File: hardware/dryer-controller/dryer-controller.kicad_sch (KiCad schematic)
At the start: 69 parts, among them K1 SRD-05VDC-SL-C, K2 SRD-05VDC-SL-C, Q1 MMBT2222A, Q2 MMBT2222A, Q3 SI2308, Q4 SI2308, Q5 SI2308, SW1 SW-USB, U1 K7805-1000R3

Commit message: Export fab files, JLCPCB BOM and CPL, and review renders
Add an export command that writes the gerber zip with drill files, a JLCPCB
BOM and CPL, the schematic PDF, a top SVG and two 3D renders from the
committed project, and copies the four review files to docs/hardware.
Mounting holes are now excluded from the BOM so the fab BOM lists only parts.
README gains an Ordering section.

Co-Authored-By: Claude Sonnet 5.5 <noreply@anthropic.com>
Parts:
- H1, H2, H3, H4: now left out of the parts list
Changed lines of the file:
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@@
 (symbol (lib_id "Connector:TestPoint") (at 177.80 254.00 0) (unit 1) (exclude_from_sim no) (in_bom yes) (on_board yes) (dnp no) (property "Reference" "TP9" (at 177.80 251.46 0) (effects (font (size 1.27 1.27)))) (property "Value" "FAN" (at 177.80 256.54 0) (effects (font (size 1.27 1.27)))) (property "Footprint" "TestPoint:TestPoint_Pad_D1.5mm" (at 177.80 254.00 0) (effects (font (size 1.27 1.27)) (hide yes))) (property "Datasheet" "~" (at 177.80 254.00 0) (effects (font (size 1.27 1.27)) (hide yes))) (property "LCSC" "" (at 177.80 254.00 0) (effects (font (size 1.27 1.27)) (hide yes))) (property "Description" "" (at 177.80 254.00 0) (effects (font (size 1.27 1.27)) (hide yes))) (pin "1") (instances (project "dryer-controller" (path "/6edf3ea2-c7c9-5bc2-9303-ad80166c5e3e" (reference "TP9") (unit 1)))))
 (global_label "FAN" (shape input) (at 177.80 254.00 270) (effects (font (size 1.27 1.27)) (justify left)))
-(symbol (lib_id "Mechanical:MountingHole") (at 215.90 254.00 0) (unit 1) (exclude_from_sim no) (in_bom yes) (on_board yes) (dnp no) (property "Reference" "H1" (at 215.90 251.46 0) (effects (font (size 1.27 1.27)))) (property "Value" "M3" (at 215.90 256.54 0) (effects (font (size 1.27 1.27)))) (property "Footprint" "MountingHole:MountingHole_3.2mm_M3" (at 215.90 254.00 0) (effects (font (size 1.27 1.27)) (hide yes))) (property "Datasheet" "~" (at 215.90 254.00 0) (effects (font (size 1.27 1.27)) (hide yes))) (property "LCSC" "" (at 215.90 254.00 0) (effects (font (size 1.27 1.27)) (hide yes))) (property "Description" "" (at 215.90 254.00 0) (effects (font (size 1.27 1.27)) (hide yes)))  (instances (project "dryer-controller" (path "/6edf3ea2-c7c9-5bc2-9303-ad80166c5e3e" (reference "H1") (unit 1)))))
-(symbol (lib_id "Mechanical:MountingHole") (at 254.00 254.00 0) (unit 1) (exclude_from_sim no) (in_bom yes) (on_board yes) (dnp no) (property "Reference" "H2" (at 254.00 251.46 0) (effects (font (size 1.27 1.27)))) (property "Value" "M3" (at 254.00 256.54 0) (effects (font (size 1.27 1.27)))) (property "Footprint" "MountingHole:MountingHole_3.2mm_M3" (at 254.00 254.00 0) (effects (font (size 1.27 1.27)) (hide yes))) (property "Datasheet" "~" (at 254.00 254.00 0) (effects (font (size 1.27 1.27)) (hide yes))) (property "LCSC" "" (at 254.00 254.00 0) (effects (font (size 1.27 1.27)) (hide yes))) (property "Description" "" (at 254.00 254.00 0) (effects (font (size 1.27 1.27)) (hide yes)))  (instances (project "dryer-controller" (path "/6edf3ea2-c7c9-5bc2-9303-ad80166c5e3e" (reference "H2") (unit 1)))))
-(symbol (lib_id "Mechanical:MountingHole") (at 292.10 254.00 0) (unit 1) (exclude_from_sim no) (in_bom yes) (on_board yes) (dnp no) (property "Reference" "H3" (at 292.10 251.46 0) (effects (font (size 1.27 1.27)))) (property "Value" "M3" (at 292.10 256.54 0) (effects (font (size 1.27 1.27)))) (property "Footprint" "MountingHole:MountingHole_3.2mm_M3" (at 292.10 254.00 0) (effects (font (size 1.27 1.27)) (hide yes))) (property "Datasheet" "~" (at 292.10 254.00 0) (effects (font (size 1.27 1.27)) (hide yes))) (property "LCSC" "" (at 292.10 254.00 0) (effects (font (size 1.27 1.27)) (hide yes))) (property "Description" "" (at 292.10 254.00 0) (effects (font (size 1.27 1.27)) (hide yes)))  (instances (project "dryer-controller" (path "/6edf3ea2-c7c9-5bc2-9303-ad80166c5e3e" (reference "H3") (unit 1)))))
-(symbol (lib_id "Mechanical:MountingHole") (at 330.20 254.00 0) (unit 1) (exclude_from_sim no) (in_bom yes) (on_board yes) (dnp no) (property "Reference" "H4" (at 330.20 251.46 0) (effects (font (size 1.27 1.27)))) (property "Value" "M3" (at 330.20 256.54 0) (effects (font (size 1.27 1.27)))) (property "Footprint" "MountingHole:MountingHole_3.2mm_M3" (at 330.20 254.00 0) (effects (font (size 1.27 1.27)) (hide yes))) (property "Datasheet" "~" (at 330.20 254.00 0) (effects (font (size 1.27 1.27)) (hide yes))) (property "LCSC" "" (at 330.20 254.00 0) (effects (font (size 1.27 1.27)) (hide yes))) (property "Description" "" (at 330.20 254.00 0) (effects (font (size 1.27 1.27)) (hide yes)))  (instances (project "dryer-controller" (path "/6edf3ea2-c7c9-5bc2-9303-ad80166c5e3e" (reference "H4") (unit 1)))))
+(symbol (lib_id "Mechanical:MountingHole") (at 215.90 254.00 0) (unit 1) (exclude_from_sim no) (in_bom no) (on_board yes) (dnp no) (property "Reference" "H1" (at 215.90 251.46 0) (effects (font (size 1.27 1.27)))) (property "Value" "M3" (at 215.90 256.54 0) (effects (font (size 1.27 1.27)))) (property "Footprint" "MountingHole:MountingHole_3.2mm_M3" (at 215.90 254.00 0) (effects (font (size 1.27 1.27)) (hide yes))) (property "Datasheet" "~" (at 215.90 254.00 0) (effects (font (size 1.27 1.27)) (hide yes))) (property "LCSC" "" (at 215.90 254.00 0) (effects (font (size 1.27 1.27)) (hide yes))) (property "Description" "" (at 215.90 254.00 0) (effects (font (size 1.27 1.27)) (hide yes)))  (instances (project "dryer-controller" (path "/6edf3ea2-c7c9-5bc2-9303-ad80166c5e3e" (reference "H1") (unit 1)))))
+(symbol (lib_id "Mechanical:MountingHole") (at 254.00 254.00 0) (unit 1) (exclude_from_sim no) (in_bom no) (on_board yes) (dnp no) (property "Reference" "H2" (at 254.00 251.46 0) (effects (font (size 1.27 1.27)))) (property "Value" "M3" (at 254.00 256.54 0) (effects (font (size 1.27 1.27)))) (property "Footprint" "MountingHole:MountingHole_3.2mm_M3" (at 254.00 254.00 0) (effects (font (size 1.27 1.27)) (hide yes))) (property "Datasheet" "~" (at 254.00 254.00 0) (effects (font (size 1.27 1.27)) (hide yes))) (property "LCSC" "" (at 254.00 254.00 0) (effects (font (size 1.27 1.27)) (hide yes))) (property "Description" "" (at 254.00 254.00 0) (effects (font (size 1.27 1.27)) (hide yes)))  (instances (project "dryer-controller" (path "/6edf3ea2-c7c9-5bc2-9303-ad80166c5e3e" (reference "H2") (unit 1)))))
+(symbol (lib_id "Mechanical:MountingHole") (at 292.10 254.00 0) (unit 1) (exclude_from_sim no) (in_bom no) (on_board yes) (dnp no) (property "Reference" "H3" (at 292.10 251.46 0) (effects (font (size 1.27 1.27)))) (property "Value" "M3" (at 292.10 256.54 0) (effects (font (size 1.27 1.27)))) (property "Footprint" "MountingHole:MountingHole_3.2mm_M3" (at 292.10 254.00 0) (effects (font (size 1.27 1.27)) (hide yes))) (property "Datasheet" "~" (at 292.10 254.00 0) (effects (font (size 1.27 1.27)) (hide yes))) (property "LCSC" "" (at 292.10 254.00 0) (effects (font (size 1.27 1.27)) (hide yes))) (property "Description" "" (at 292.10 254.00 0) (effects (font (size 1.27 1.27)) (hide yes)))  (instances (project "dryer-controller" (path "/6edf3ea2-c7c9-5bc2-9303-ad80166c5e3e" (reference "H3") (unit 1)))))
+(symbol (lib_id "Mechanical:MountingHole") (at 330.20 254.00 0) (unit 1) (exclude_from_sim no) (in_bom no) (on_board yes) (dnp no) (property "Reference" "H4" (at 330.20 251.46 0) (effects (font (size 1.27 1.27)))) (property "Value" "M3" (at 330.20 256.54 0) (effects (font (size 1.27 1.27)))) (property "Footprint" "MountingHole:MountingHole_3.2mm_M3" (at 330.20 254.00 0) (effects (font (size 1.27 1.27)) (hide yes))) (property "Datasheet" "~" (at 330.20 254.00 0) (effects (font (size 1.27 1.27)) (hide yes))) (property "LCSC" "" (at 330.20 254.00 0) (effects (font (size 1.27 1.27)) (hide yes))) (property "Description" "" (at 330.20 254.00 0) (effects (font (size 1.27 1.27)) (hide yes)))  (instances (project "dryer-controller" (path "/6edf3ea2-c7c9-5bc2-9303-ad80166c5e3e" (reference "H4") (unit 1)))))
 (symbol (lib_id "power:PWR_FLAG") (at 368.30 254.00 0) (unit 1) (exclude_from_sim no) (in_bom no) (on_board yes) (dnp no) (property "Reference" "#FLG1" (at 368.30 251.46 0) (effects (font (size 1.27 1.27)))) (property "Value" "PWR_FLAG" (at 368.30 256.54 0) (effects (font (size 1.27 1.27)))) (property "Footprint" "" (at 368.30 254.00 0) (effects (font (size 1.27 1.27)) (hide yes))) (property "Datasheet" "~" (at 368.30 254.00 0) (effects (font (size 1.27 1.27)) (hide yes))) (property "LCSC" "" (at 368.30 254.00 0) (effects (font (size 1.27 1.27)) (hide yes))) (property "Description" "" (at 368.30 254.00 0) (effects (font (size 1.27 1.27)) (hide yes))) (pin "1") (instances (project "dryer-controller" (path "/6edf3ea2-c7c9-5bc2-9303-ad80166c5e3e" (reference "#FLG1") (unit 1)))))
 (global_label "+24V" (shape input) (at 368.30 254.00 270) (effects (font (size 1.27 1.27)) (justify left)))

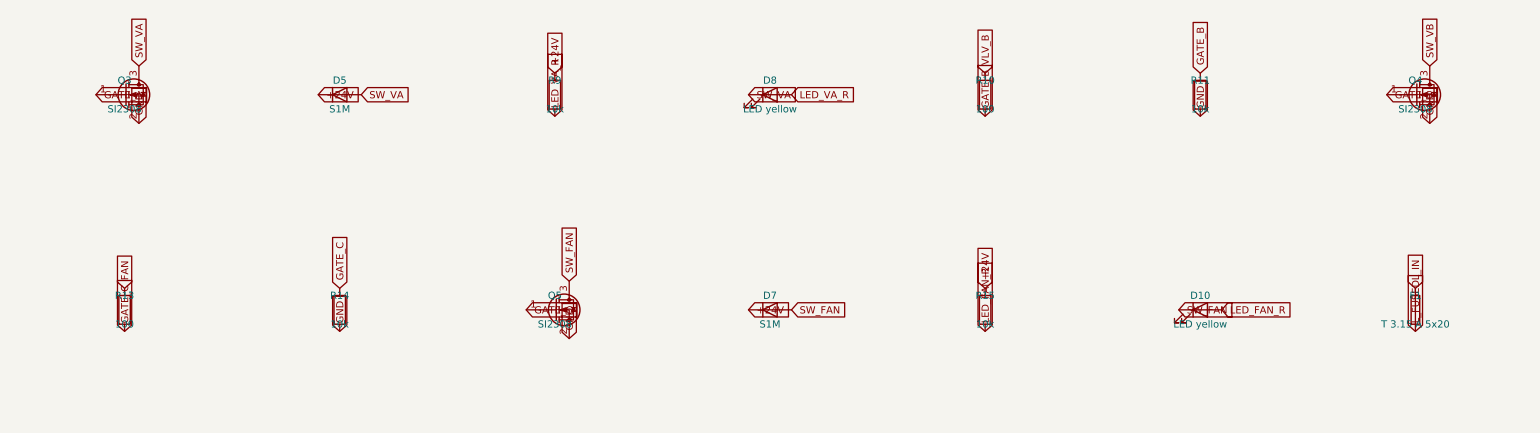
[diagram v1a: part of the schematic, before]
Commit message: Pin every part to an LCSC number and settle the switch, fuse holder and header footprints
Every part in circuit.py now carries a JLCPCB/LCSC number. Its description
names the maker part and says whether it is basic or extended. The numbers
were looked up on 2026-10-14 and all of them offer assembly. U1 is
hand-fitted: MornSun's K7805-1000R3 is not stocked at LCSC or Mouser, and
the TRACO TSR 1-2450 the footprint is drawn for is named as the source.
The catalogue test is no longer an expected failure.

The DORABO pluggable headers, the pin header and the sockets match their
stock KiCad footprints in pitch, pin count and hole size, so those stay.
Two parts get local footprints:
- SW1 is a SOFNG SS-12D00-G3, which has a 2.5 mm pitch.
- F1 is an XFCN PTF-76-B covered holder with pins 15 mm apart. Those pins
  land on the existing L_IN and L_FUSED track ends at (77, 7) and (92, 7).
  A 22 mm holder would have come within 6 mm of H2.
The only change to the mains copper is that the old clip's dangling
L_FUSED stub to x 97 goes.

TP2 moves 0.1 mm left to x 37.4. At 37.5 the re-routed board trips a
KiCad 10 DRC false positive on GND fill around TP2 and its via. The saved
fill keeps 0.3 mm there.

Scratch projects (the tests) now get a copy of the local footprints, so
their ERC resolves dryer: footprints. Datasheets for the new parts go
under docs/datasheets (new connectors/ and fuses/ groups), with README
rows. The mating plugs are listed in hardware/README.md.

Co-Authored-By: Claude Opus 5.5 <noreply@anthropic.com>
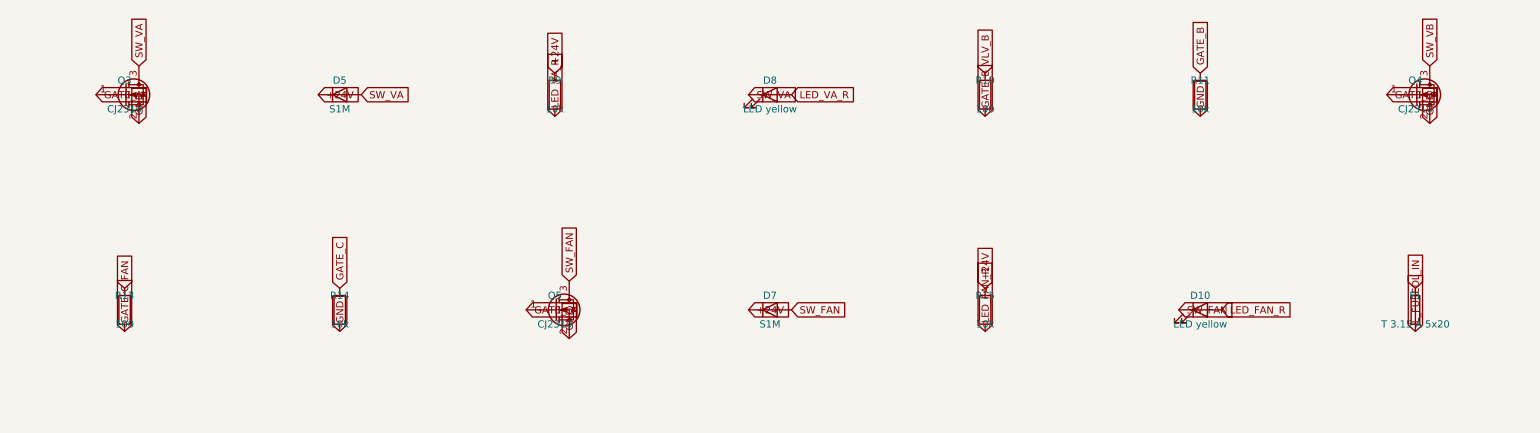
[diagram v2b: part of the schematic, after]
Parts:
- C1: LCSC (none) -> C294509
- C2: LCSC (none) -> C440198
- C3: LCSC (none) -> C45783
- C4: LCSC (none) -> C231174
- C5: LCSC (none) -> C49678
- C6: LCSC (none) -> C15850
- D1, D2, D5, D6, D7: LCSC (none) -> C95872
- D10, D8, D9: LCSC (none) -> C2296
- D11, D14: LCSC (none) -> C8678
- D12, D13: LCSC (none) -> C2297
- D3, D4: LCSC (none) -> C84256
- F1: footprint Fuse:Fuseholder_Clip-5x20mm_Littelfuse_111_Inline_P20.00x5.00mm_D1.05mm_Horizontal -> dryer:Fuseholder_5x20mm_Covered_XFCN_PTF-76-B_P15.00mm; LCSC (none) -> C48603682
- F2: LCSC (none) -> C142747
- J_24V: LCSC (none) -> C395734
- J_DISP: LCSC (none) -> C492407
- J_ESP12: LCSC (none) -> C2905419
- J_ESP16: LCSC (none) -> C2905421
- J_LOADS: LCSC (none) -> C395768
- J_MAINS: LCSC (none) -> C395786
- J_SENS: LCSC (none) -> C430559
- Q1, Q2: LCSC (none) -> C8512
- Q3, Q4, Q5: value SI2308 -> CJ2310; LCSC (none) -> C75882
- R1, R2, R4, R5: LCSC (none) -> C17513
- R10, R13, R7: LCSC (none) -> C17408
- R11, R12, R14, R15, R16, R8, R9: LCSC (none) -> C17414
- R17, R3, R6: LCSC (none) -> C17520
- R18: LCSC (none) -> C27834
- SW1: footprint Button_Switch_THT:SW_Slide_SPDT_Straight_CK_OS102011MS2Q -> dryer:SW_Slide_SPDT_SOFNG_SS-12D00_P2.50mm; LCSC (none) -> C22355741
- U1: Hand fit (none) -> yes

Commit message: Drill the pluggable headers to their datasheet holes and clear F1 off the slot
The DORABO headers have square pins: 1.0 mm on the 5.08 mm parts and
0.8 mm on the 3.5 mm part. Their drawings ask for Ø1.7 and Ø1.4 holes,
because the pin's diagonal governs. The stock Phoenix footprints drill
1.4 and 1.2. Local copies of the four Phoenix footprints now carry the
datasheet drills, with pads widened to keep a 0.3 mm ring:
- the 5.08 mm headers: 2.3 x 3.6 mm pads, 2.78 mm between pad edges;
- J_SENS: 2.0 x 3.6 mm pads.

F1 moves 0.3 mm right to (77.3, 7) so its body clears the slot. Its L_IN
pad now sits 6.3 mm from the SELV pour instead of exactly 6.0. The L_IN
and L_FUSED track ends follow it. The placement comment now states the
mains-to-SELV invariant as copper-edge distances.

Co-Authored-By: Claude Opus 5.5 <noreply@anthropic.com>
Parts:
- J_24V: footprint Connector_Phoenix_MSTB:PhoenixContact_MSTBVA_2,5_2-G-5,08_1x02_P5.08mm_Vertical -> dryer:PhoenixContact_MSTBVA_2,5_2-G-5,08_1x02_P5.08mm_Vertical_Drill1.7mm
- J_LOADS: footprint Connector_Phoenix_MSTB:PhoenixContact_MSTBVA_2,5_6-G-5,08_1x06_P5.08mm_Vertical -> dryer:PhoenixContact_MSTBVA_2,5_6-G-5,08_1x06_P5.08mm_Vertical_Drill1.7mm
- J_MAINS: footprint Connector_Phoenix_MSTB:PhoenixContact_MSTBA_2,5_8-G-5,08_1x08_P5.08mm_Horizontal -> dryer:PhoenixContact_MSTBA_2,5_8-G-5,08_1x08_P5.08mm_Horizontal_Drill1.7mm
- J_SENS: footprint Connector_Phoenix_MC:PhoenixContact_MCV_1,5_9-G-3.5_1x09_P3.50mm_Vertical -> dryer:PhoenixContact_MCV_1,5_9-G-3.5_1x09_P3.50mm_Vertical_Drill1.4mm

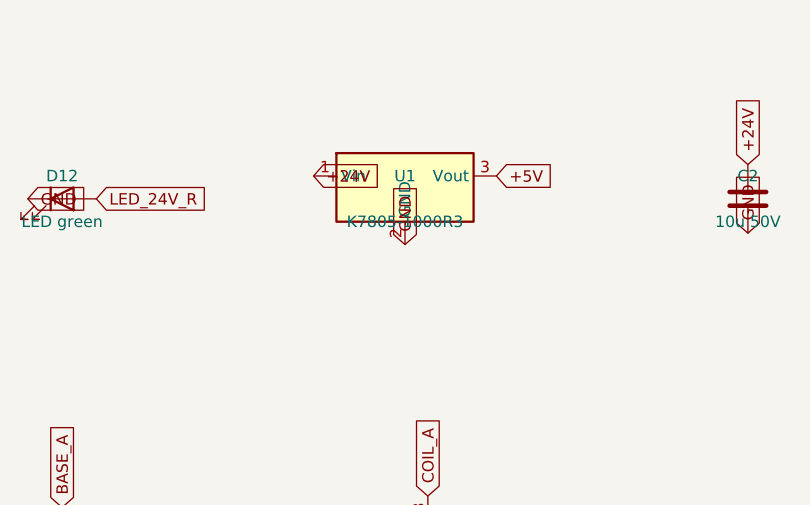
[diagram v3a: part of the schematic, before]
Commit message: Make the fab-order files match what is fitted
U1's value was K7805-1000R3 while the fitted part is the TRACO TSR 1-2450
from Mouser; the value is now TSR 1-2450 and the description names the
Mouser source and the MornSun part as the unstocked alternative. The
hardware.md BOM row follows.

Test points TP1-TP9 were in the BOM with no LCSC number, contradicting
"test points are not parts"; the schematic now marks them not in BOM, so
the BOM designators equal the CPL's exactly and every BOM line but U1
carries an LCSC number (both tests red on the old schematic).

The release step attached out/*.csv, which picks up KiCad's own position
file; it now attaches the -bom and -cpl files only, and releasing.md
drops the position-CSV wording. kicad/kicad:10.0.6 exists on Docker Hub,
so CI pins it: the TP2 placement works round a DRC false positive seen
in 10.0.6.

Co-Authored-By: Claude Opus 5.5 <noreply@anthropic.com>
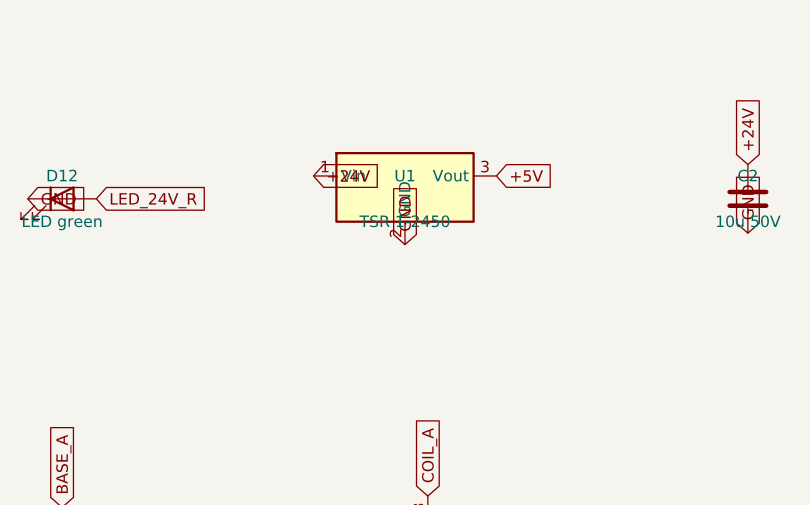
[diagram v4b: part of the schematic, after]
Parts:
- TP1, TP2, TP3, TP4, TP5, TP6, TP7, TP8, TP9: now left out of the parts list
- U1: value K7805-1000R3 -> TSR 1-2450
